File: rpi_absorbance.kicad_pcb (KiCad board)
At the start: 2 copper layers, 36 parts, among them CON1 BARREL_JACK, P1 CONN_02X04, P2 CONN_01X02, P3 RPI_HEADER, P4 STEPPER_CONN, P5 CONN_02X04, Q1 ZTX692B, U1 R-78B5.0-1.5L, U2 MUN5216DW1T1G, U3 DRV8825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

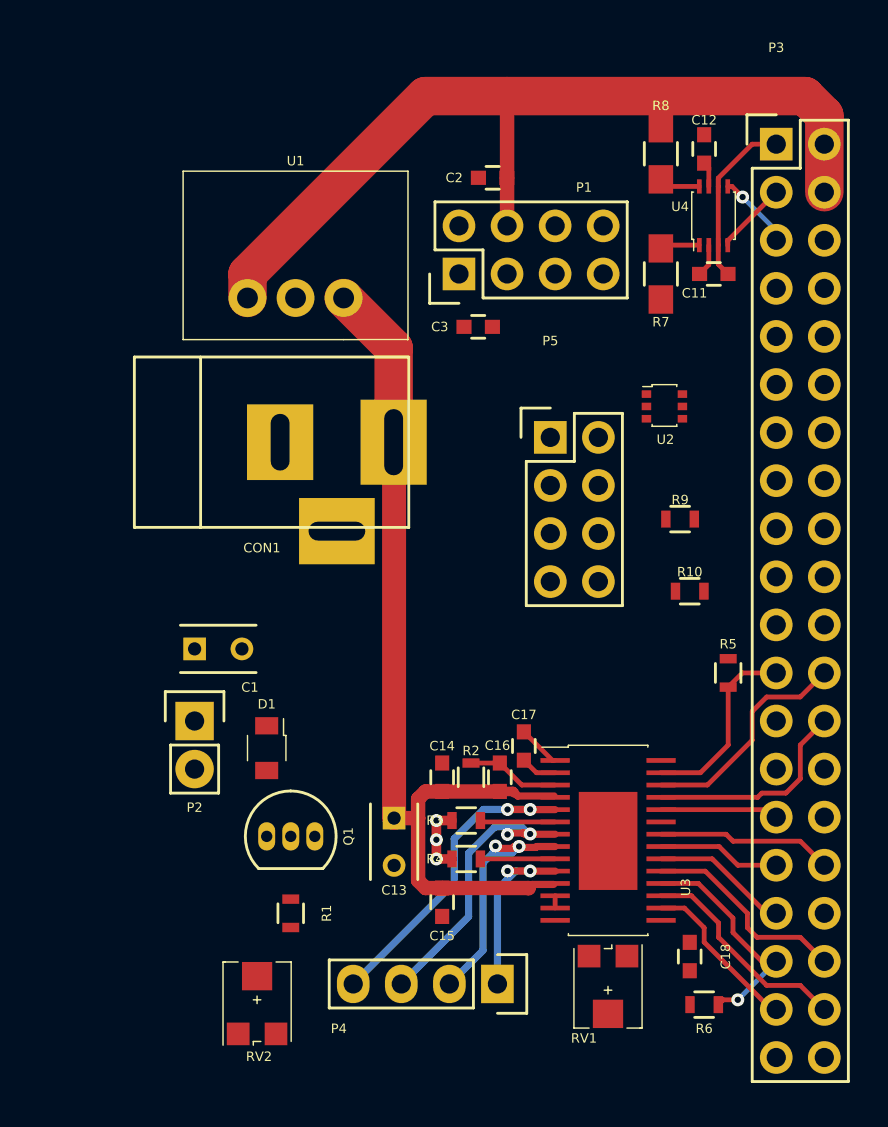
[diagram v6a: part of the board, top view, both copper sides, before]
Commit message: Improve pcb layout, change capacitor footprints
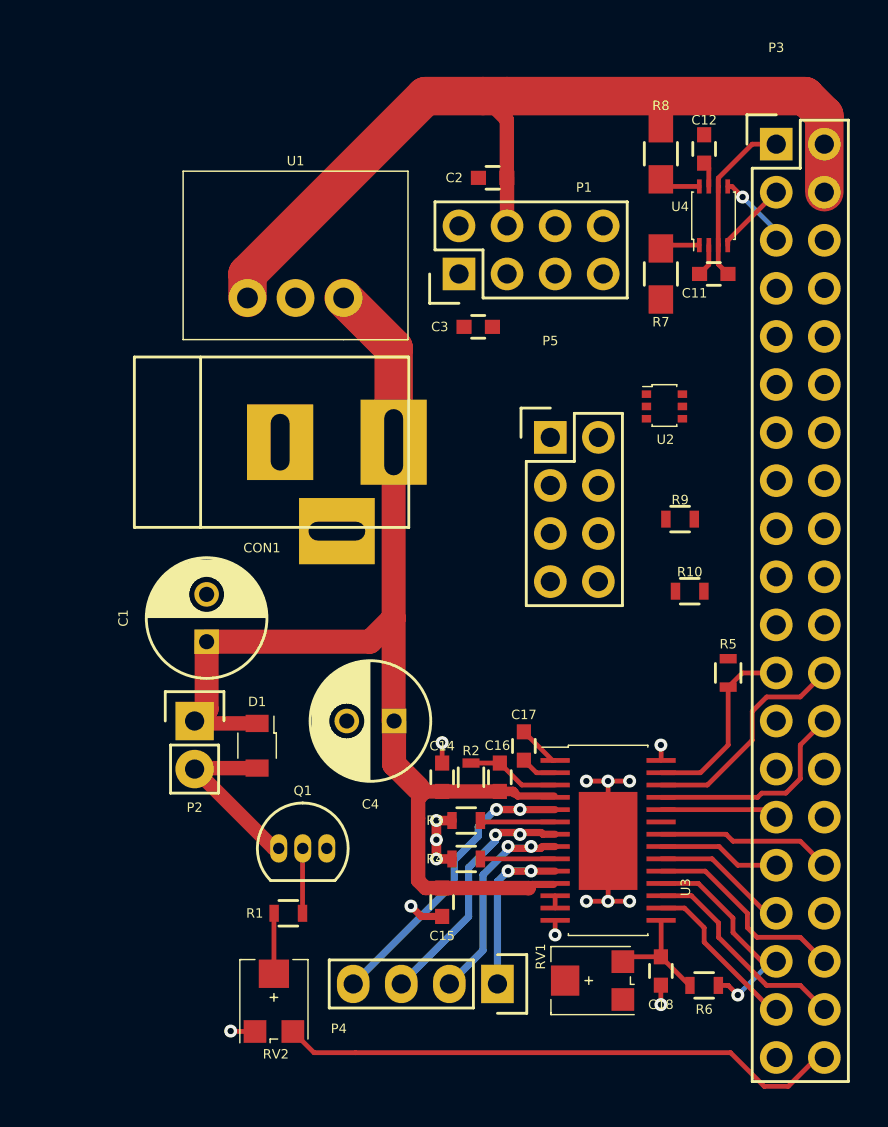
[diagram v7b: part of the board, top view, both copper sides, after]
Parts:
- removed C13: 100u, Capacitors_ThroughHole:C_Rect_L4_W2.5_P2.5
- added C4: 100u, Capacitors_ThroughHole:C_Radial_D6.3_L11.2_P2.5, F.Cu at (159.4, 125.5)
- C1: footprint Capacitors_ThroughHole:C_Rect_L4_W2.5_P2.5 -> Capacitors_ThroughHole:C_Radial_D6.3_L11.2_P2.5
- moved C18 1.70 mm to (173.5, 138.7)
- moved RV1 1.14 mm to (169.7, 139.2), turned to 90 degrees
- moved R6 1.02 mm to (175.8, 139.4)
- moved RV2 0.90 mm to (153.0, 140.1)
- moved Q1 0.90 mm to (153.3, 132.2)
- moved C1 0.74 mm to (149.5, 121.3), turned to 90 degrees
- moved D1 0.52 mm to (152.1, 125.6)
- moved R1 0.13 mm to (153.8, 135.6), turned to 180 degrees
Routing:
- net /PERI: track 0.00 -> 29.9 mm
- net GND: track 6.43 -> 24.2 mm, vias 3 -> 15
- net +12V: track 49.2 -> 65.1 mm
- net Net-(D1-Pad2): track 0.00 -> 9.50 mm
- net /V3P3: track 0.00 -> 6.21 mm
- net Net-(Q1-Pad2): track 0.00 -> 3.43 mm
- net Net-(R1-Pad2): track 0.00 -> 3.20 mm
- net +5V: track 49.8 -> 48.8 mm

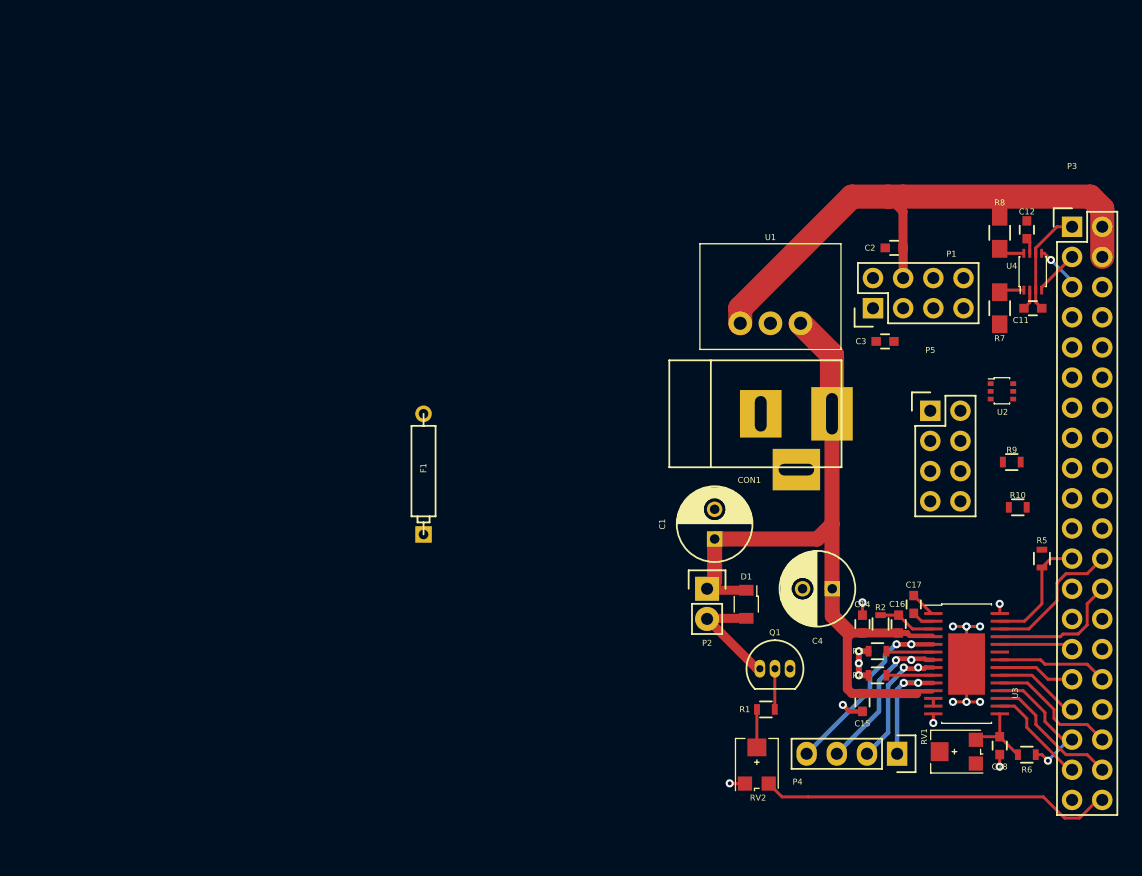
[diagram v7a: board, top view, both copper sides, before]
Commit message: Add LED transistor layout
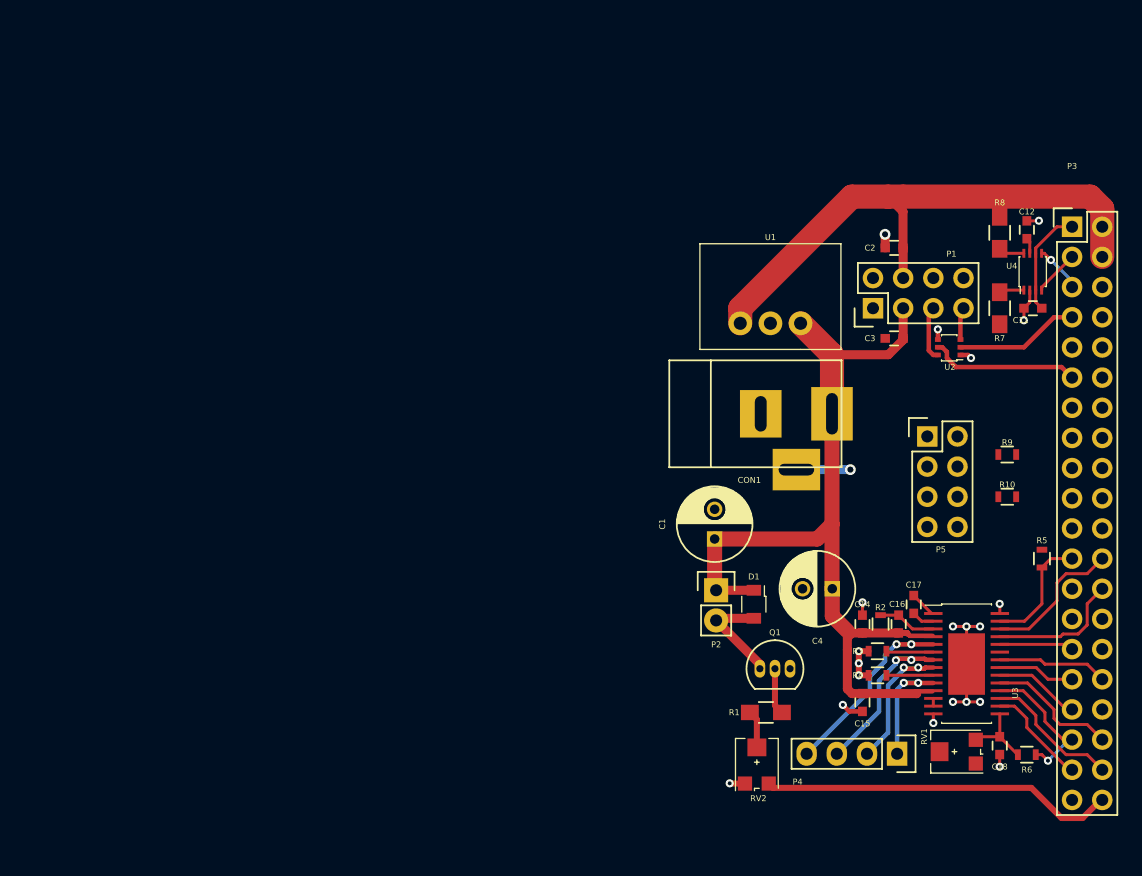
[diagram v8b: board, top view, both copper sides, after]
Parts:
- removed F1: F_Small, Discret:CP4
- R1: footprint Resistors_SMD:R_0603 -> Resistors_SMD:R_0805_HandSoldering
- moved U2 3.50 mm to (170.2, 105.8), turned to 180 degrees
- moved P5 2.17 mm to (167.4, 112.6)
- moved R10 1.26 mm to (174.1, 117.7)
- moved C3 0.80 mm to (164.6, 104.4)
- moved P2 0.77 mm to (149.6, 125.6)
- moved R9 0.74 mm to (174.1, 114.2)
- moved D1 0.64 mm to (152.8, 125.6)
- moved R1 0.25 mm to (153.8, 135.9)
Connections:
- C3 pad 2: Net-(C3-Pad2) -> +12V
- P1 pad 3: Net-(C3-Pad2) -> +12V
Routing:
- net /LED2: track 0.00 -> 12.7 mm
- net /LED1: track 0.00 -> 10.4 mm
- net GND: track 24.2 -> 33.8 mm, vias 15 -> 21
- net +12V: track 65.1 -> 74.1 mm
- net Net-(P1-Pad5): track 0.00 -> 4.64 mm
- net Net-(P1-Pad7): track 0.00 -> 2.74 mm
- net Net-(D1-Pad2): track 9.50 -> 8.84 mm
- net Net-(Q1-Pad2): track 3.43 -> 3.94 mm
